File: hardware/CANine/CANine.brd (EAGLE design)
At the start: 15.2 x 37.9 mm, 23 parts, among them J1 UJ2-MIBH2-4-SMT-TR, J5 DF13A-4P-1.25H(21), U1 STM32F042C6T6, U2 AP2202K-3.3TRG1, U3 MCP2551

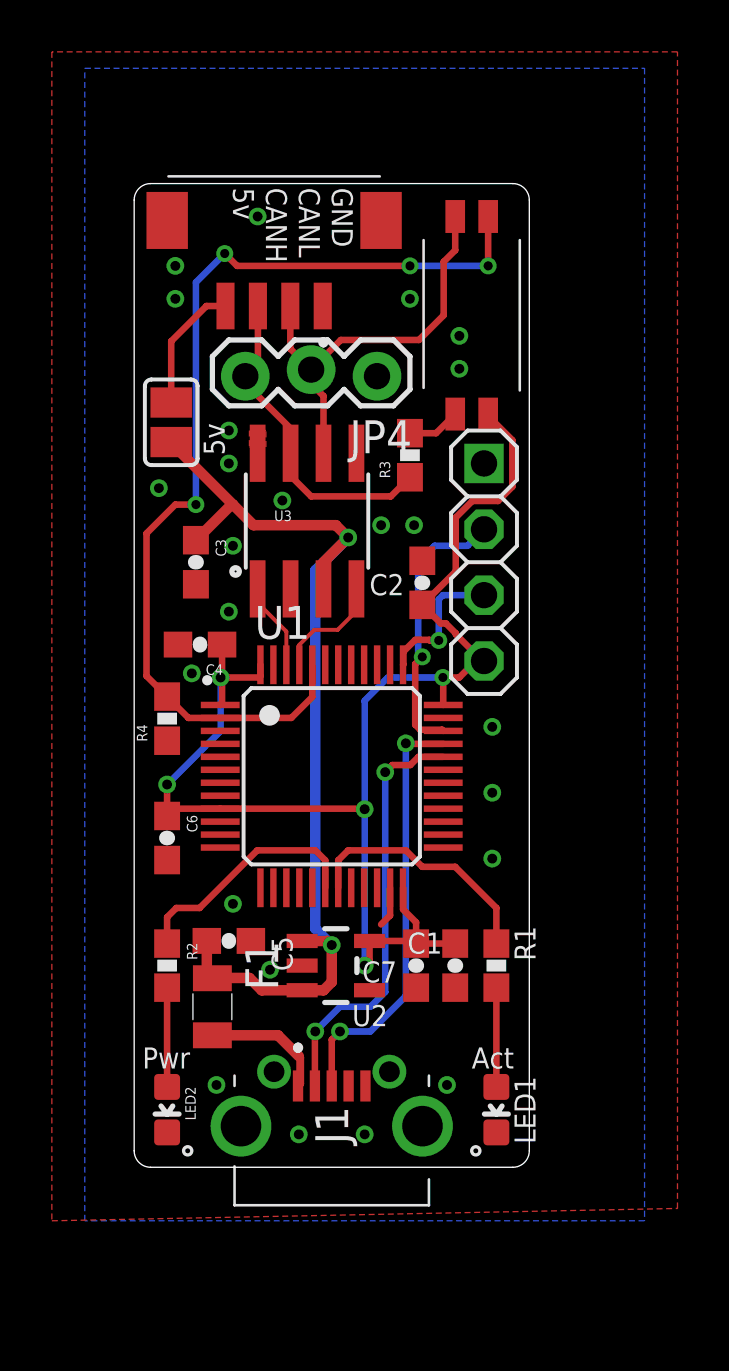
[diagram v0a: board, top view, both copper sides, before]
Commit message: Update CANine CAN Adapter schematics and models (#77)
* update can adapter

* update case
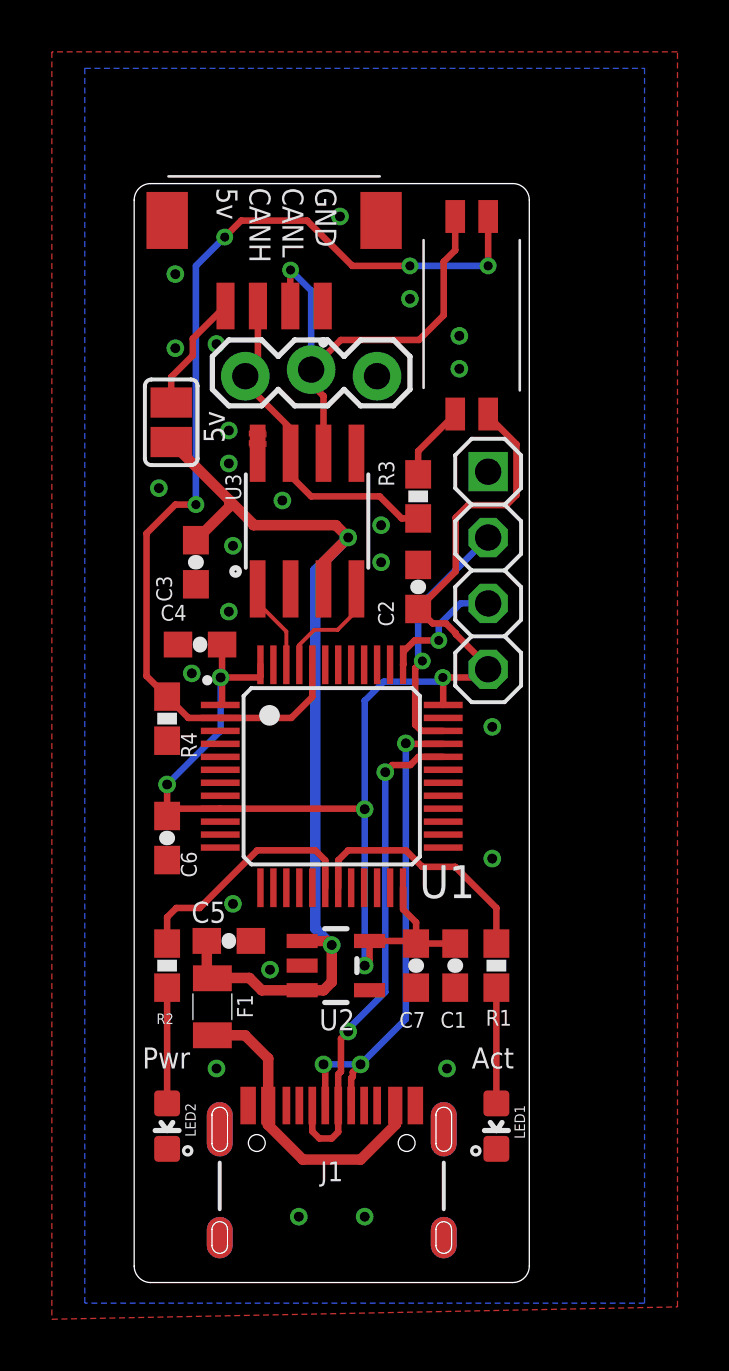
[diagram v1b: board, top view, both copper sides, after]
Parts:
- J1: value UJ2-MIBH2-4-SMT-TR -> (none); device SamacSys_Parts:UJ2MIBH24SMTTR -> USB-C-Breakout:SPARKFUN-CONNECTORS_USB-C-16P
- LED1: value BLUE -> KW DELSS2.RA-AXBZ-FK0PM0-2686
- LED2: value GREEN -> KW DELSS2.RA-AXBZ-FK0PM0-2686
- R3: value 120 -> RC0603JR-7W120RL
- moved R3 1.62 mm to (11.6, 26.0)
- moved J1 1.27 mm to (8.26, 2.54), turned to 0 degrees
- moved LED1 0.64 mm to (14.6, 1.75)
- moved LED2 0.64 mm to (1.91, 1.75)
- moved JP1 0.35 mm to (14.3, 23.2)
- moved C2 0.22 mm to (11.6, 22.5)
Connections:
- removed net N$7: F1.2, J1.1
- new net VBUS_USB: F1.2, J1.VBUS1, J1.VBUS2
- net D+: now also J1.A6, J1.B6; no longer J1.3
- net D-: now also J1.A7, J1.B7; no longer J1.2
- net GND: now also J1.GND, J1.GND2; no longer J1.5
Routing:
- net VBUS_USB: track 0.00 -> 11.9 mm
- net N$7: track 4.87 -> 0.00 mm
- net D-: track 16.4 -> 19.3 mm
- net D+: track 16.5 -> 19.3 mm, vias 2 -> 3
- net CANL: track 16.2 -> 19.0 mm, vias 0 -> 1
- net GND: track 1.56 -> 0.00 mm
- net BOOT0: track 38.9 -> 40.3 mm
- net 3.3V: track 54.7 -> 55.8 mm
- net SWDIO: track 10.7 -> 9.69 mm
- net N$3: track 2.05 -> 2.92 mm
- net N$23: track 3.83 -> 4.46 mm
- net N$2: track 3.83 -> 4.46 mm
- net SWCLK: track 5.47 -> 4.90 mm
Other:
- board size 15.2 x 37.9 mm -> 15.2 x 42.4 mm
